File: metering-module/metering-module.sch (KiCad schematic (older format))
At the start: 25 parts, among them J1 North, J2 South, Q1 MMBT3904, Q2 MMBT3904, U1 LTV-817S, U2 LTV-817S, U3 BA033CC0FP-E2, U4 MAX3486, U5 MAX3486

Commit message: Ongoing
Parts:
- added J3: West, Connector_PinHeader_2.54mm:PinHeader_1x14_P2.54mm_Vertical, symbol Connector_Generic:Conn_01x14
- added J4: East, Connector_PinHeader_2.54mm:PinHeader_1x14_P2.54mm_Vertical, symbol Connector_Generic:Conn_01x14
- added J5: RJ12, Connector_RJ:RJ12_Amphenol_54601, symbol Connector:RJ12
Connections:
- wire segments 79 -> 85
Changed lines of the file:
@@
+	1    0    0    -1
+$EndComp
+$Comp
+L Connector_Generic:Conn_01x14 J3
+U 1 1 61A75369
+P 7850 3900
+F 0 "J3" H 7930 3892 50  0000 L CNN
+F 1 "West" H 7930 3801 50  0000 L CNN
+F 2 "Connector_PinHeader_2.54mm:PinHeader_1x14_P2.54mm_Vertical" H 7850 3900 50  0001 C CNN
+F 3 "~" H 7850 3900 50  0001 C CNN
+	1    7850 3900
+	1    0    0    -1
+$EndComp
+$Comp
+L Connector_Generic:Conn_01x14 J4
+U 1 1 61A769CA
+P 10100 3900
+F 0 "J4" H 10180 3892 50  0000 L CNN
+F 1 "East" H 10180 3801 50  0000 L CNN
+F 2 "Connector_PinHeader_2.54mm:PinHeader_1x14_P2.54mm_Vertical" H 10100 3900 50  0001 C CNN
+F 3 "~" H 10100 3900 50  0001 C CNN
+	1    10100 3900
+	1    0    0    -1
+$EndComp
+$Comp
+L power:+3V3 #PWR0120
+U 1 1 61A79F7D
+P 7500 3150
+F 0 "#PWR0120" H 7500 3000 50  0001 C CNN
+F 1 "+3V3" H 7515 3323 50  0000 C CNN
+F 2 "" H 7500 3150 50  0001 C CNN
+F 3 "" H 7500 3150 50  0001 C CNN
+	1    7500 3150
+	1    0    0    -1
+$EndComp
+$Comp
+L power:GND #PWR0121
+U 1 1 61A7D923
+P 9250 4850
+F 0 "#PWR0121" H 9250 4600 50  0001 C CNN
+F 1 "GND" H 9255 4677 50  0000 C CNN
+F 2 "" H 9250 4850 50  0001 C CNN
+F 3 "" H 9250 4850 50  0001 C CNN
+	1    9250 4850
+	1    0    0    -1
+$EndComp
+$Comp
+L power:GNDPWR #PWR0122
+U 1 1 61A7E0B7
+P 9750 5000
+F 0 "#PWR0122" H 9750 4800 50  0001 C CNN
+F 1 "GNDPWR" H 9754 4846 50  0000 C CNN
+F 2 "" H 9750 4950 50  0001 C CNN
+F 3 "" H 9750 4950 50  0001 C CNN
+	1    9750 5000
+	1    0    0    -1
+$EndComp
+Wire Wire Line
+	9750 4600 9900 4600
+Wire Wire Line
+	9900 3300 9250 3300
+Wire Wire Line
+	9250 3300 9250 4850
+Wire Wire Line
+	7500 3150 7500 3300
+Wire Wire Line
+	7500 3300 7650 3300
+Wire Wire Line
+	9750 4600 9750 5000
+$Comp
+L Connector:RJ12 J5
+U 1 1 61AB8295
+P 4600 6200
+F 0 "J5" H 4657 6767 50  0000 C CNN
+F 1 "RJ12" H 4657 6676 50  0000 C CNN
+F 2 "Connector_RJ:RJ12_Amphenol_54601" V 4600 6225 50  0001 C CNN
+F 3 "~" V 4600 6225 50  0001 C CNN
+	1    4600 6200
 	1    0    0    -1
 $EndComp

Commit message: Ongoing Work
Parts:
- removed H1, H2: MountingHole_Pad, MountingHole:MountingHole_4.3mm_M4, symbol Mechanical:MountingHole_Pad
- removed J5: RJ12, Connector_RJ:RJ12_Amphenol_54601, symbol Connector:RJ12
- added C5, C6: 100nF, Capacitor_SMD:C_1206_3216Metric_Pad1.33x1.80mm_HandSolder, symbol Device:C
- added D5, D6, D7, D8: D_TVS, Diode_SMD:D_0603_1608Metric_Pad1.05x0.95mm_HandSolder, symbol Device:D_TVS
- added R10, R11, R6, R7, R8, R9: R, Resistor_SMD:R_1206_3216Metric_Pad1.30x1.75mm_HandSolder, symbol Device:R
- added TP1: Shield, TestPoint:TestPoint_Pad_D4.0mm, symbol Connector:TestPoint
- C2: value C -> 100nF
- R5: value R -> 10k
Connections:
- net labels added: RS485_1_A, RS485_1_B, S0_0, S0_1
- wire segments 85 -> 126
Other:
- moved on the sheet: J1, J2, J3, J4

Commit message: Ongoing Work. Still not ready for small and dedicated commits.
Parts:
- removed D5, D6: D_TVS, Diode_SMD:D_0603_1608Metric_Pad1.05x0.95mm_HandSolder, symbol Device:D_TVS
- removed R6, R7: R, Resistor_SMD:R_1206_3216Metric_Pad1.30x1.75mm_HandSolder, symbol Device:R
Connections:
- net GND: now also J1.1 (Pin_1), J1.3 (Pin_3), J2.3 (Pin_3); no longer J2.2 (Pin_2)
- net GNDPWR: now also J2.4 (Pin_4)
- net RS485_0_RX: now also J3.4 (Pin_4); no longer U4.1 (RO)
- net RS485_0_TX: now also J3.10 (Pin_10); no longer U4.4 (DI)
- net RS485_0_TXE: now also J3.9 (Pin_9); no longer U4.2 (~RE), U4.3 (DE)
- net S0_0: now also J1.4 (Pin_4), J3.5 (Pin_5)
- net S0_1: now also J1.2 (Pin_2), J3.12 (Pin_12)
- net SW0: now also J3.13 (Pin_13)
- net SW1: now also J4.10 (Pin_10)
- net VCC: now also J2.2 (Pin_2)
- net RS485_1_RX: now reaches J3.6 (Pin_6)
- net RS485_1_RX: now also U4.1 (RO)
- net RS485_1_TXE: now reaches J4.12 (Pin_12)
- net RS485_1_TXE: now also U4.2 (~RE), U4.3 (DE)
- net RS485_1_TX: now reaches J4.13 (Pin_13)
- net RS485_1_TX: now also U4.4 (DI)
- net U0TXD: now reaches J4.4 (Pin_4)
- net U0RXD: now reaches J4.5 (Pin_5)
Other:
- moved on the sheet: J1, J2, J3, J4, TP1

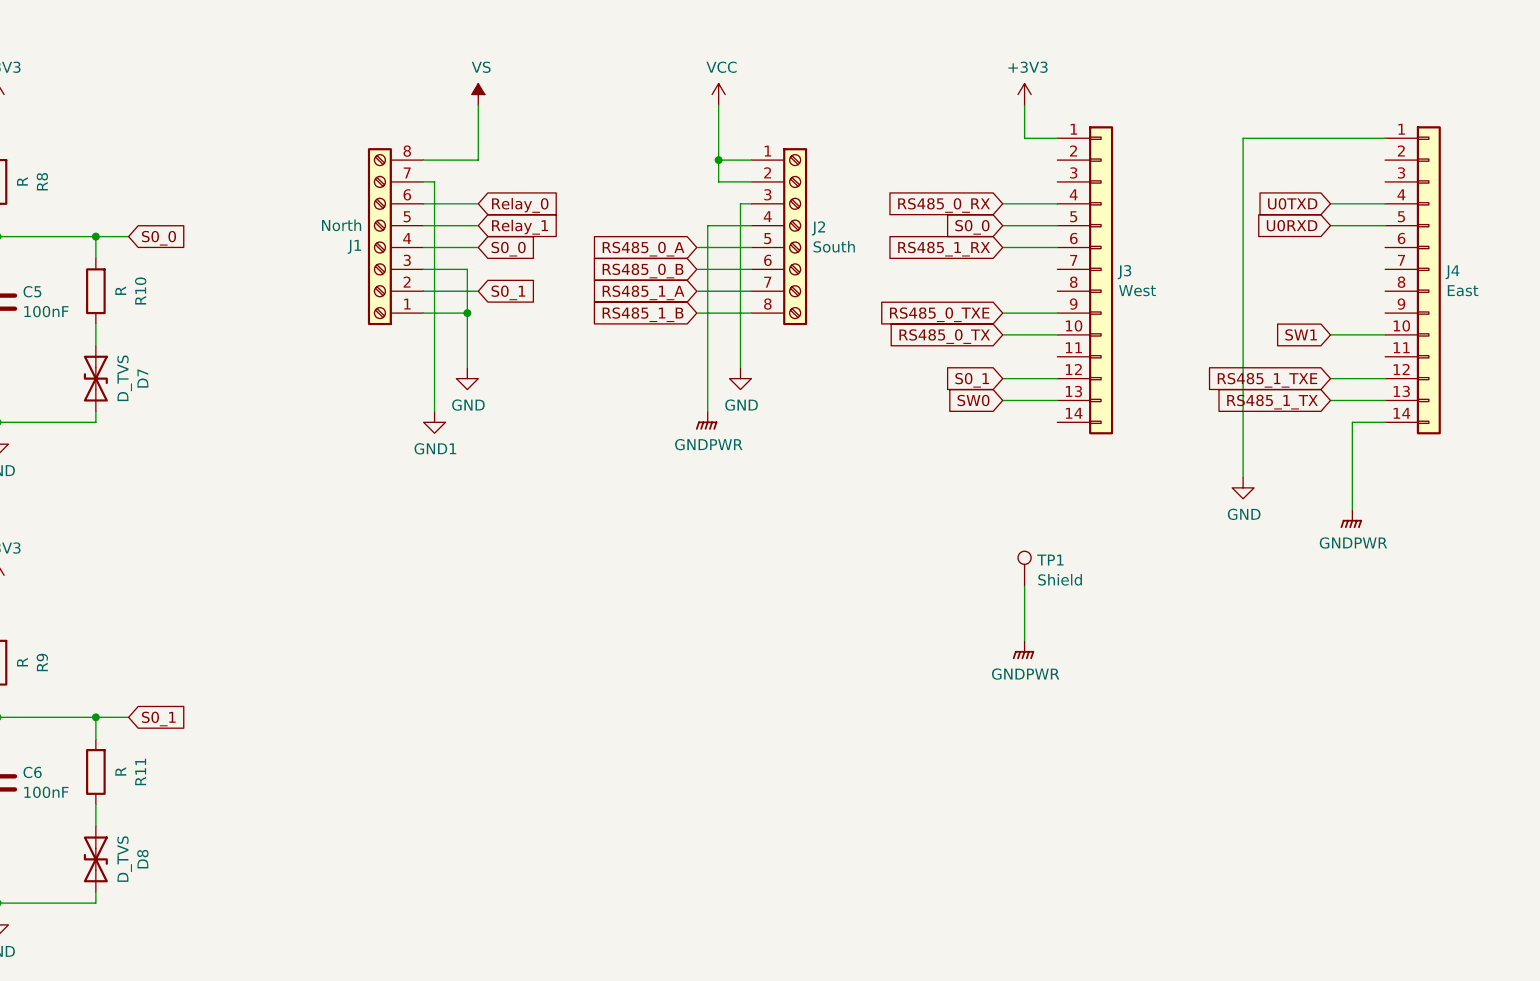
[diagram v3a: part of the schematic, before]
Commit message: Use a GPIO expander for metering module to safe pins
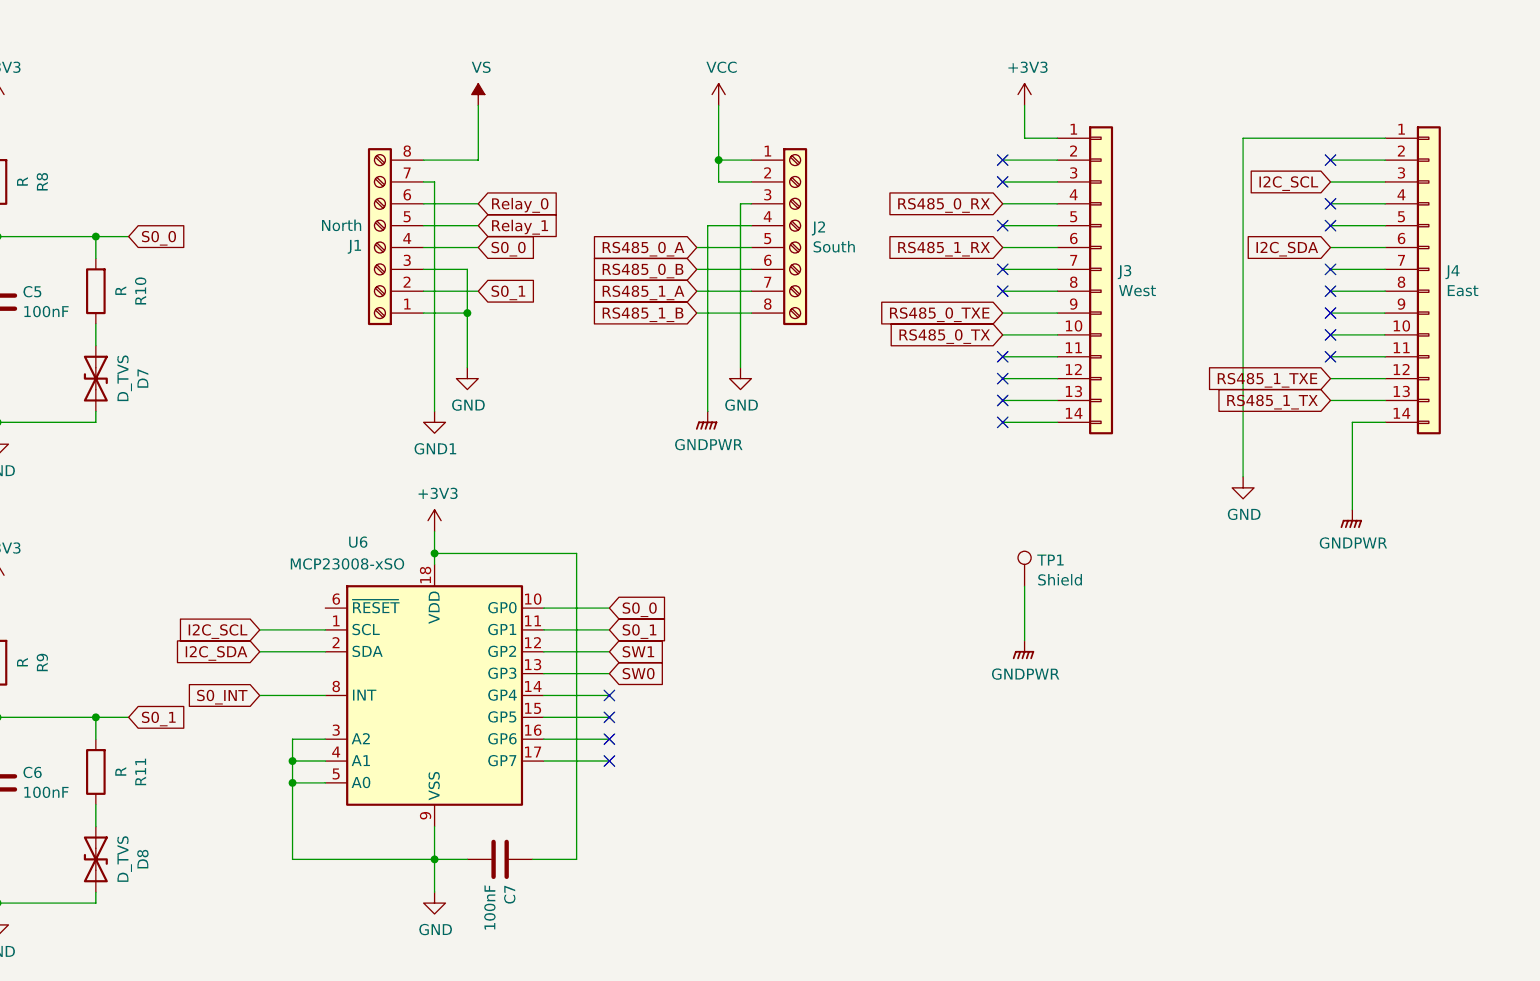
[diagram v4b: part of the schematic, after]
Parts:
- added C7: 100nF, Capacitor_SMD:C_1206_3216Metric_Pad1.33x1.80mm_HandSolder, symbol Device:C
- added U6: MCP23008-xSO, Package_SO:SOIC-18W_7.5x11.6mm_P1.27mm, symbol Interface_Expansion:MCP23008-xSO
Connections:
- net +3V3: now also C7.1, U6.18 (VDD)
- net GND: now also C7.2, U6.3 (A2), U6.4 (A1), U6.5 (A0), U6.9 (VSS)
- net S0_0: now also U6.10 (GP0); no longer J3.5 (Pin_5)
- net S0_1: now also U6.11 (GP1); no longer J3.12 (Pin_12)
- net SW0: now also U6.13 (GP3); no longer J3.13 (Pin_13)
- net SW1: now also U6.12 (GP2); no longer J4.10 (Pin_10)
- net I2C_SCL: now reaches J4.3 (Pin_3)
- net I2C_SCL: now also U6.1 (SCL)
- net I2C_SDA: now reaches J4.6 (Pin_6)
- net I2C_SDA: now also U6.2 (SDA)
- net U0RXD: no longer names the net of J4.5 (Pin_5)
- net U0TXD: no longer names the net of J4.4 (Pin_4)
- new net S0_INT: U6.8 (INT)
- no-connect marks 0 -> 21
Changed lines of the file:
@@
 Wire Wire Line
 	7000 4000 7150 4000
-Text GLabel 9800 4100 0    50   Input ~ 0
-U0TXD
-Text GLabel 9800 4200 0    50   Input ~ 0
-U0RXD
 Wire Wire Line
 	9800 4100 10050 4100
@@
 Wire Wire Line
 	7000 3650 7000 3900
-Text GLabel 8300 4200 0    50   Input ~ 0
+Text GLabel 6500 5950 2    50   Input ~ 0
 S0_0
-Text GLabel 8300 4900 0    50   Input ~ 0
+Text GLabel 6500 6050 2    50   Input ~ 0
 S0_1
-Text GLabel 8300 5000 0    50   Input ~ 0
+Text GLabel 6500 6250 2    50   Input ~ 0
 SW0
-Text GLabel 9800 4700 0    50   Input ~ 0
+Text GLabel 6500 6150 2    50   Input ~ 0
 SW1
 Wire Wire Line
@@
 Wire Wire Line
 	5850 4600 5850 4850
+$Comp
+L Interface_Expansion:MCP23008-xSO U6
+U 1 1 61EB4389
+P 5700 6350
+F 0 "U6" H 5350 7050 50  0000 C CNN
+F 1 "MCP23008-xSO" H 5300 6950 50  0000 C CNN
+F 2 "Package_SO:SOIC-18W_7.5x11.6mm_P1.27mm" H 5700 5300 50  0001 C CNN
+F 3 "http://ww1.microchip.com/downloads/en/DeviceDoc/MCP23008-MCP23S08-Data-Sheet-20001919F.pdf" H 7000 5150 50  0001 C CNN
+	1    5700 6350
+	1    0    0    -1
+$EndComp
+$Comp
+L Device:C C7
+U 1 1 61F32AD8
+P 6000 7100
+F 0 "C7" H 6115 7146 50  0000 L CNN
+F 1 "100nF" H 6115 7055 50  0000 L CNN
+F 2 "Capacitor_SMD:C_1206_3216Metric_Pad1.33x1.80mm_HandSolder" H 6038 6950 50  0001 C CNN
+F 3 "~" H 6000 7100 50  0001 C CNN
+	1    6000 7100
+	0    1    1    0
+$EndComp
+$Comp
+L power:+3V3 #PWR0127
+U 1 1 61F36D22
+P 5700 5600
+F 0 "#PWR0127" H 5700 5450 50  0001 C CNN
+F 1 "+3V3" H 5715 5773 50  0000 C CNN
+F 2 "" H 5700 5600 50  0001 C CNN
+F 3 "" H 5700 5600 50  0001 C CNN
+	1    5700 5600
+	1    0    0    -1
+$EndComp
+$Comp
+L power:GND #PWR0133
+U 1 1 61F37FD9
+P 5700 7250
+F 0 "#PWR0133" H 5700 7000 50  0001 C CNN
+F 1 "GND" H 5705 7077 50  0000 C CNN
+F 2 "" H 5700 7250 50  0001 C CNN
+F 3 "" H 5700 7250 50  0001 C CNN
+	1    5700 7250
+	1    0    0    -1
+$EndComp
+Wire Wire Line
+	5700 5600 5700 5700
+Wire Wire Line
+	5700 6950 5700 7100
+Wire Wire Line
+	5850 7100 5700 7100
+Connection ~ 5700 7100
+Wire Wire Line
+	5700 7100 5700 7250
+Wire Wire Line
+	6150 7100 6350 7100
+Wire Wire Line
+	6350 7100 6350 5700
+Wire Wire Line
+	6350 5700 5700 5700
+Connection ~ 5700 5700
+Wire Wire Line
+	5700 5700 5700 5750
+NoConn ~ 9800 4700
+NoConn ~ 8300 4900
+NoConn ~ 8300 5000
+NoConn ~ 8300 4200
+Wire Wire Line
+	6200 5950 6500 5950
+Wire Wire Line
+	6200 6050 6500 6050
+Wire Wire Line
+	6500 6150 6200 6150
+Wire Wire Line
+	6200 6250 6500 6250
+NoConn ~ 6500 6350
+NoConn ~ 6500 6450
+NoConn ~ 6500 6550
+NoConn ~ 6500 6650
+Wire Wire Line
+	6500 6350 6200 6350
+Wire Wire Line
+	6500 6450 6200 6450
+Wire Wire Line
+	6500 6550 6200 6550
+Wire Wire Line
+	6500 6650 6200 6650
+Text GLabel 4900 6150 0    50   Input ~ 0
+I2C_SDA
+Text GLabel 4900 6050 0    50   Input ~ 0
+I2C_SCL
+Text GLabel 9800 4300 0    50   Input ~ 0
+I2C_SDA
+Text GLabel 9800 4000 0    50   Input ~ 0
+I2C_SCL
+Wire Wire Line
+	9800 4000 10050 4000
+Wire Wire Line
+	9800 4300 10050 4300
+NoConn ~ 8300 4000
+NoConn ~ 8300 3900
+NoConn ~ 8300 4400
+NoConn ~ 8300 4500
+NoConn ~ 8300 4800
+NoConn ~ 8300 5100
+NoConn ~ 9800 4800
+NoConn ~ 9800 4600
+NoConn ~ 9800 4500
+NoConn ~ 9800 4400
+NoConn ~ 9800 4200
+NoConn ~ 9800 4100
+NoConn ~ 9800 3900
+Wire Wire Line
+	8300 3900 8550 3900
+Wire Wire Line
+	8300 4000 8550 4000
+Wire Wire Line
+	8300 4400 8550 4400
+Wire Wire Line
+	8300 4500 8550 4500
+Wire Wire Line
+	8300 4800 8550 4800
+Wire Wire Line
+	8300 5100 8550 5100
+Wire Wire Line
+	9800 3900 10050 3900
+Wire Wire Line
+	9800 4400 10050 4400
+Wire Wire Line
+	9800 4500 10050 4500
+Wire Wire Line
+	9800 4600 10050 4600
+Wire Wire Line
+	9800 4800 10050 4800
+Wire Wire Line
+	4900 6050 5200 6050
+Wire Wire Line
+	4900 6150 5200 6150
+Text GLabel 4900 6350 0    50   Input ~ 0
+S0_INT
+Wire Wire Line
+	4900 6350 5200 6350
+Wire Wire Line
+	5200 6550 5050 6550
+Wire Wire Line
+	5050 6550 5050 6650
+Wire Wire Line
+	5050 7100 5700 7100
+Wire Wire Line
+	5050 6650 5200 6650
+Connection ~ 5050 6650
+Wire Wire Line
+	5050 6650 5050 6750
+Wire Wire Line
+	5200 6750 5050 6750
+Connection ~ 5050 6750
+Wire Wire Line
+	5050 6750 5050 7100
 $EndSCHEMATC
